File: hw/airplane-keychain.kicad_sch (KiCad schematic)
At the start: 25 parts, among them SW1 SW_PUSH, SW2 SPST, U1 ATtiny85-20P

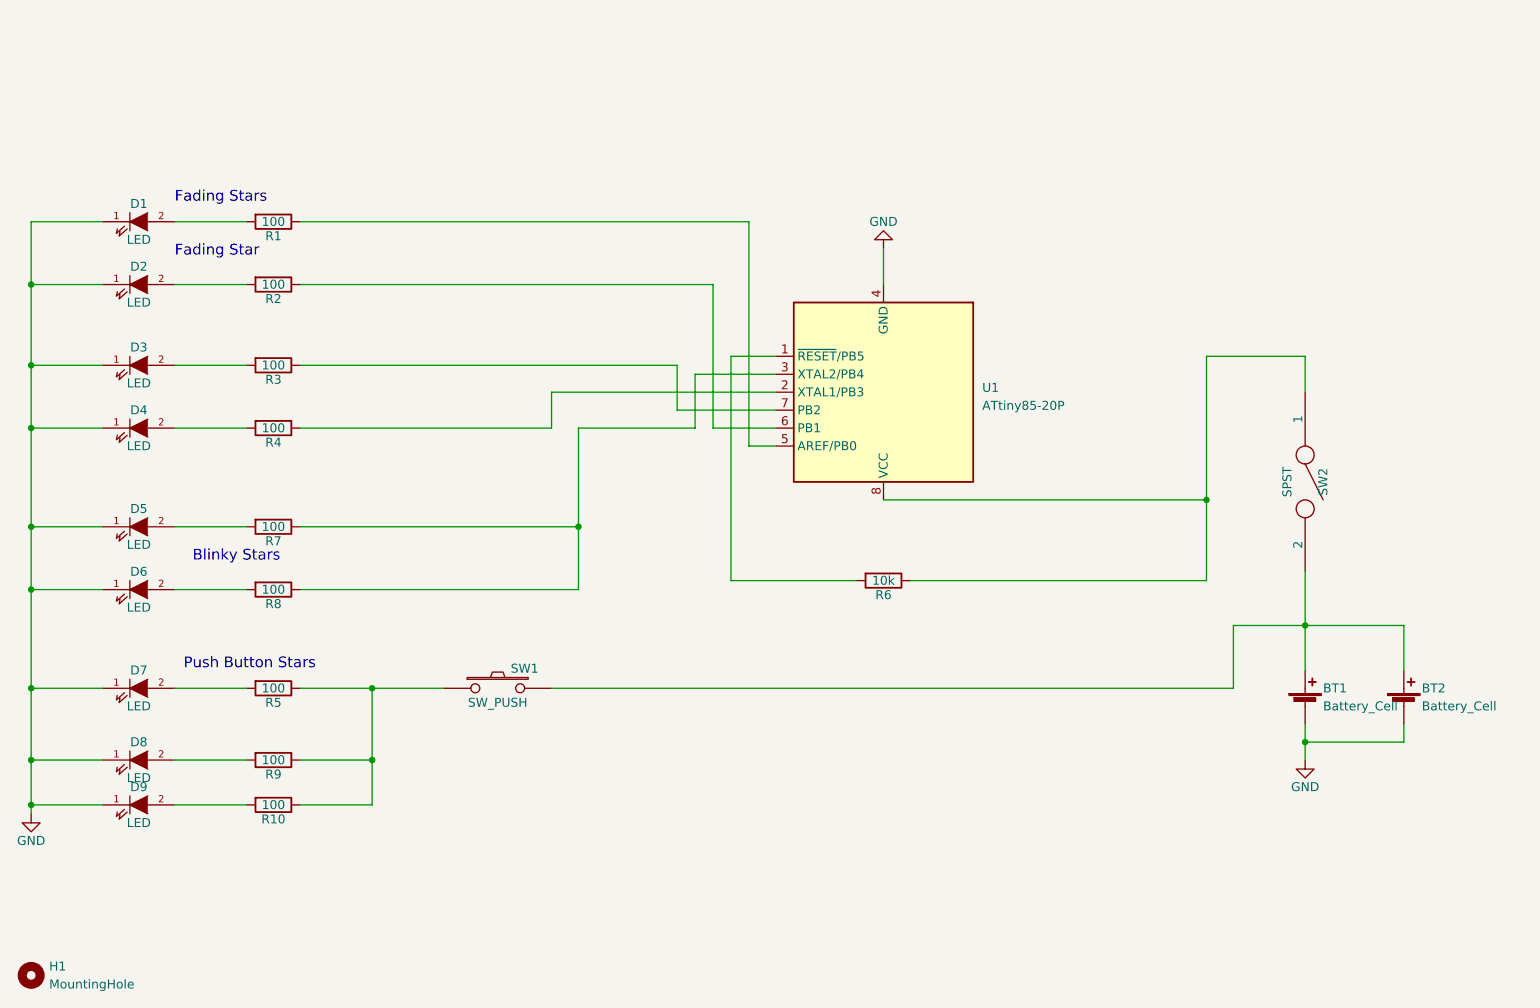
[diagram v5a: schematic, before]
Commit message: Rev B
Removed some components
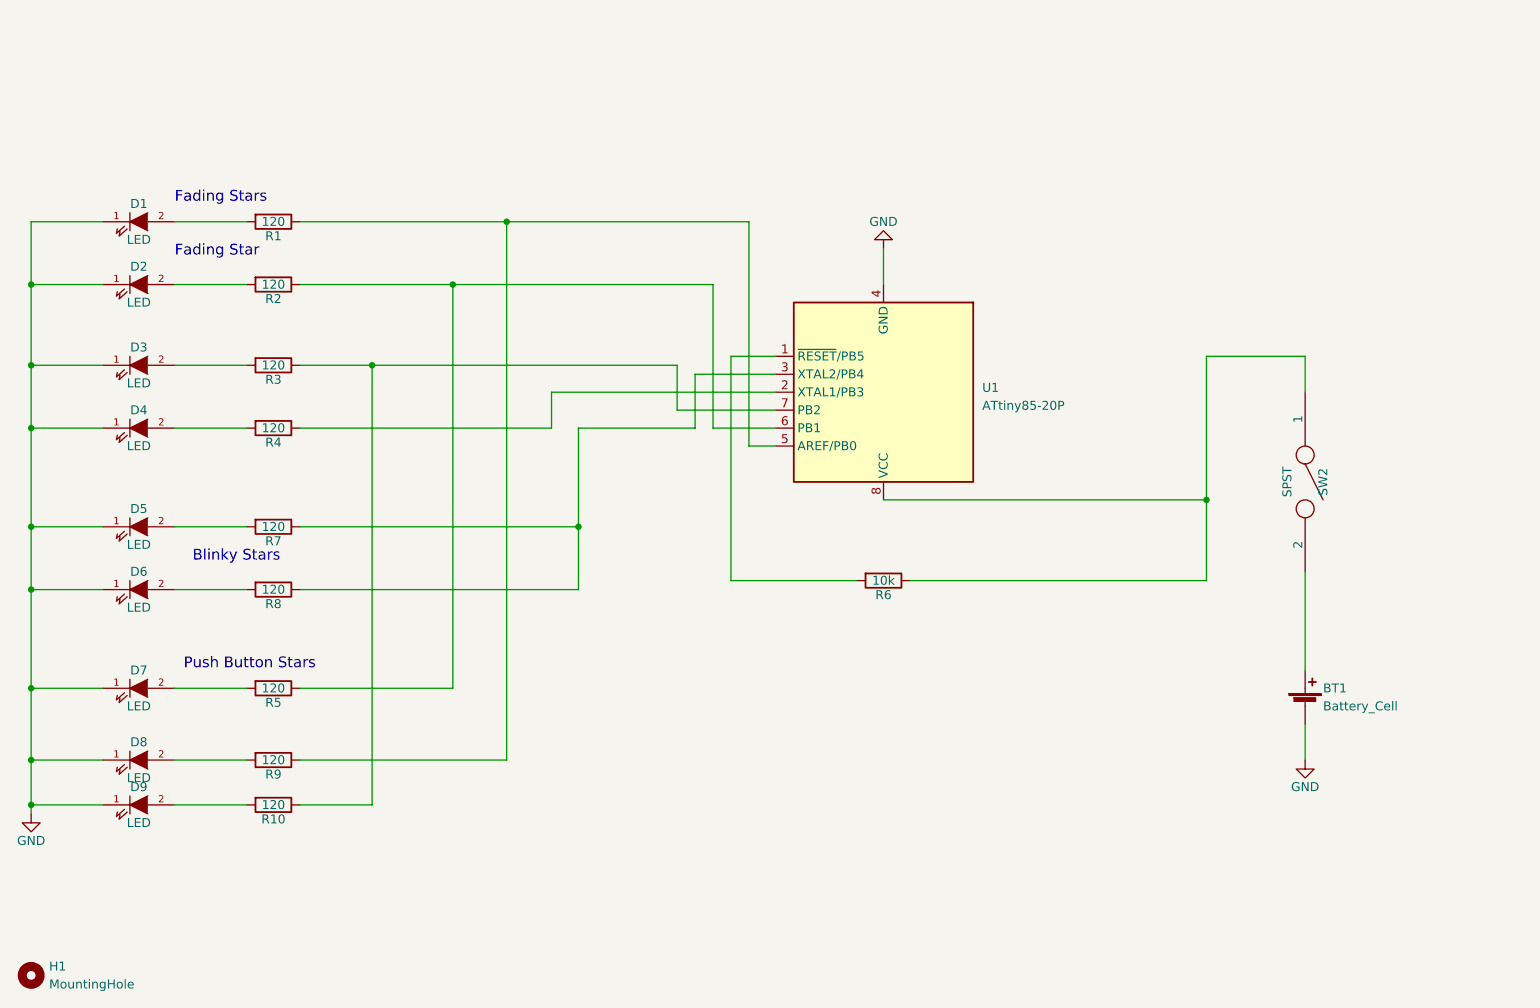
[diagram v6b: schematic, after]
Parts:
- removed BT2: Battery_Cell, Battery:BatteryHolder_Keystone_1058_1x2032, symbol airplane-keychain-rescue:Battery_Cell
- removed SW1: SW_PUSH, Button_Switch_THT:SW_PUSH_6mm, symbol airplane-keychain-rescue:SW_PUSH
- R1, R10, R2, R3, R4, R5, R7, R8, R9: value 100 -> 120
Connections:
- net at R1.1, U1.5 (AREF/PB0): now also R9.1
- net at R2.1, U1.6 (PB1): now also R5.1
- net at R3.1, U1.7 (PB2): now also R10.1

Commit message: M2I Version
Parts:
- removed D7, D8, D9: LED, LED_THT:LED_D3.0mm, symbol airplane-keychain-rescue:LED-RESCUE-airplane-keychain
- removed R10, R5, R9: 120, Resistor_THT:R_Axial_DIN0309_L9.0mm_D3.2mm_P12.70mm_Horizontal, symbol airplane-keychain-rescue:R

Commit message: update
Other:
- title: ISGC Keychain -> M2I Challenge Coin
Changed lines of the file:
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@@
 	(paper "A4")
 	(title_block
-		(title "ISGC Keychain")
-		(date "2025-03-26")
+		(title "M2I Challenge Coin")
+		(date "2025-11-24")
 		(rev "B")
 		(company "Make to Innovate")
 		(comment 1 "Matthew E. Nelson")
-		(comment 2 "ISGC Badge")
 	)
 	(text "Fading Star"
